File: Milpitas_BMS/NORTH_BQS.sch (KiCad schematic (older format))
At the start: 91 parts, among them U300 BQ79606

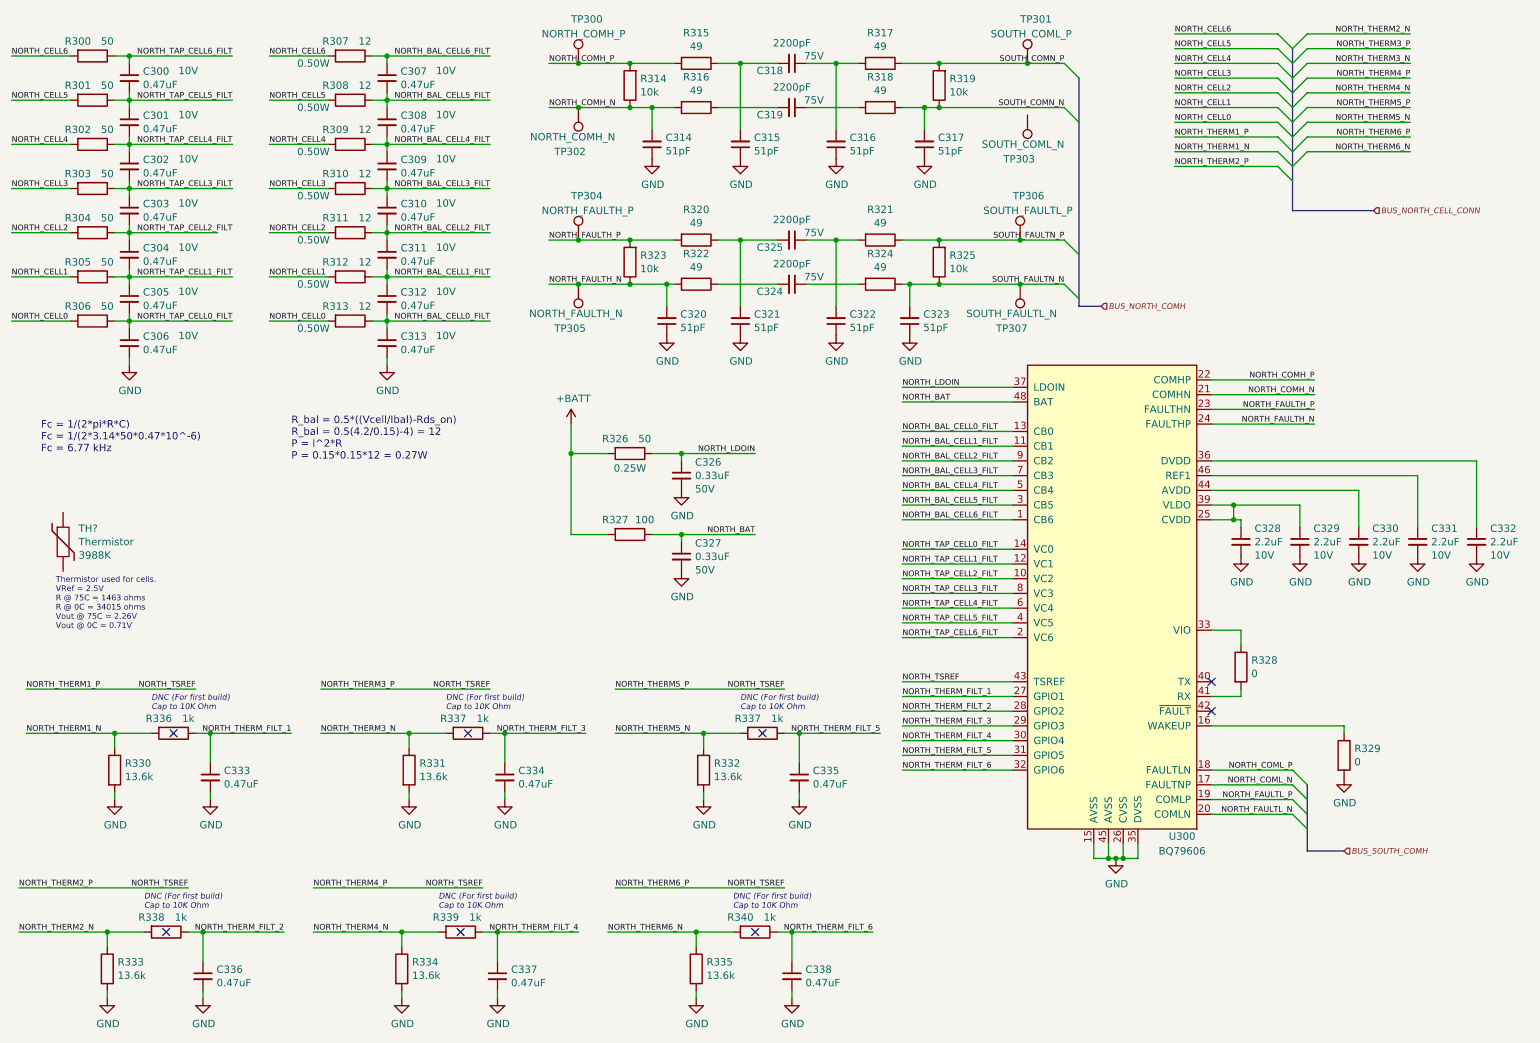
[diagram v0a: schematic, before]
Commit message: updated some parts to inclued footprints + digikey P/N
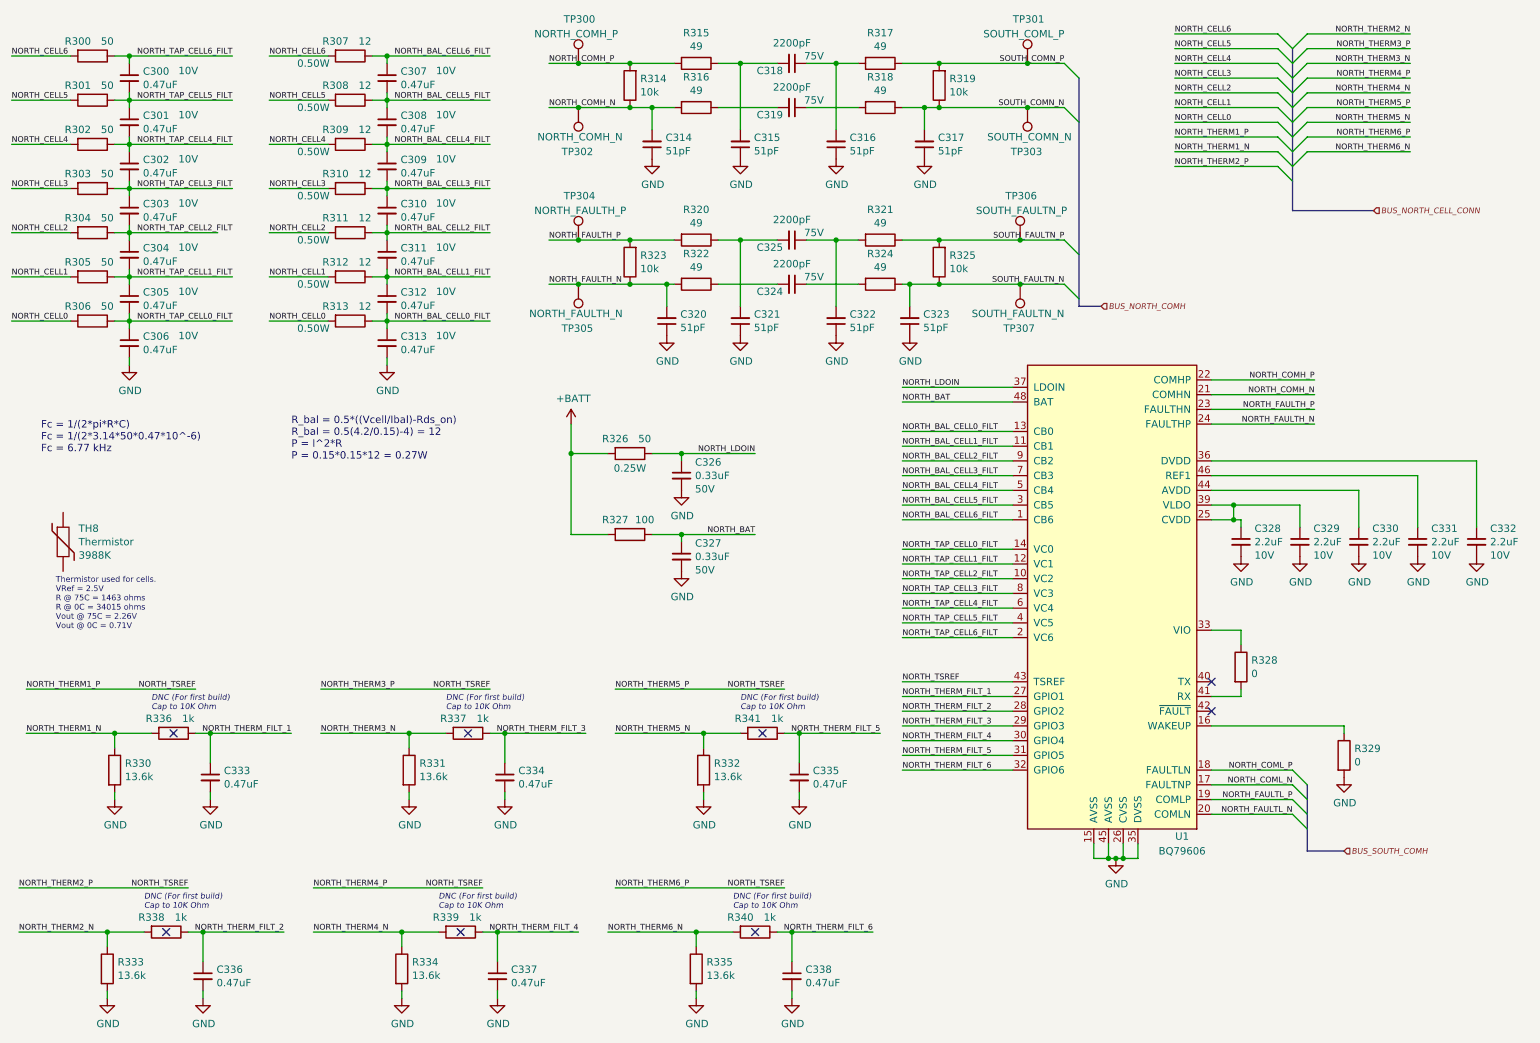
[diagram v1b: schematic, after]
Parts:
- removed U300: BQ79606, symbol Milipitas:BQ79606
- added U1: BQ79606, Package_QFP:LQFP-48-1EP_7x7mm_P0.5mm_EP3.6x3.6mm_ThermalVias, symbol Milipitas:BQ79606
- C300, C301, C302, C303, C304, C305, C306, C307, C308, C309, C310, C311, C312, C313, C314, C315, C316, C317, C318, C319, C320, C321, C322, C323, C324, C325, C326, C327, C328, C329, C330, C331, C332, C333, C334, C335, C336, C337, C338: footprint (none) -> Capacitor_SMD:C_0603_1608Metric
- R307, R308, R309, R310, R311, R312, R313, R314, R315, R316, R317, R318, R319, R320, R321, R322, R323, R324, R325, R326, R327, R328, R329, R336, R337, R338, R339, R340: footprint (none) -> Resistor_SMD:R_0603_1608Metric
- R341: renamed from R337; footprint (none) -> Resistor_SMD:R_0603_1608Metric
- TP300, TP301, TP302, TP304, TP305: footprint (none) -> TestPoint:TestPoint_Bridge_Pitch2.54mm_Drill1.0mm; Digikey (none) -> 36-5003-ND
- TP303: value SOUTH_COML_N -> SOUTH_COMN_N; footprint (none) -> TestPoint:TestPoint_Bridge_Pitch2.54mm_Drill1.0mm; Digikey (none) -> 36-5003-ND
- TP306: value SOUTH_FAULTL_P -> SOUTH_FAULTN_P; footprint (none) -> TestPoint:TestPoint_Bridge_Pitch2.54mm_Drill1.0mm; Digikey (none) -> 36-5003-ND
- TP307: value SOUTH_FAULTL_N -> SOUTH_FAULTN_N; footprint (none) -> TestPoint:TestPoint_Bridge_Pitch2.54mm_Drill1.0mm; Digikey (none) -> 36-5003-ND
- gave numbers to parts that had none: 1
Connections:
- net GND: now also U1.15 (AVSS), U1.26 (CVSS), U1.35 (DVSS), U1.45 (AVSS)
- net NORTH_BAL_CELL0_FILT: now also U1.13 (CB0)
- net NORTH_BAL_CELL1_FILT: now also U1.11 (CB1)
- net NORTH_BAL_CELL2_FILT: now also U1.9 (CB2)
- net NORTH_BAL_CELL3_FILT: now also U1.7 (CB3)
- net NORTH_BAL_CELL4_FILT: now also U1.5 (CB4)
- net NORTH_BAL_CELL5_FILT: now also U1.3 (CB5)
- net NORTH_BAL_CELL6_FILT: now also U1.1 (CB6)
- net NORTH_BAT: now also U1.48 (BAT)
- net NORTH_COMH_N: now also U1.21 (COMHN)
- net NORTH_COMH_P: now also U1.22 (COMHP)
- net NORTH_COML_N: now also U1.17 (FAULTNP)
- net NORTH_COML_P: now also U1.18 (FAULTLN)
- net NORTH_FAULTH_N: now also U1.24 (FAULTHP)
- net NORTH_FAULTH_P: now also U1.23 (FAULTHN)
- net NORTH_FAULTL_N: now also U1.20 (COMLN)
- net NORTH_FAULTL_P: now also U1.19 (COMLP)
- net NORTH_LDOIN: now also U1.37 (LDOIN)
- net NORTH_TAP_CELL0_FILT: now also U1.14 (VC0)
- net NORTH_TAP_CELL1_FILT: now also U1.12 (VC1)
- net NORTH_TAP_CELL2_FILT: now also U1.10 (VC2)
- net NORTH_TAP_CELL3_FILT: now also U1.8 (VC3)
- net NORTH_TAP_CELL4_FILT: now also U1.6 (VC4)
- net NORTH_TAP_CELL5_FILT: now also U1.4 (VC5)
- net NORTH_TAP_CELL6_FILT: now also U1.2 (VC6)
- net NORTH_THERM1_P: now also U1.43 (TSREF)
- net NORTH_THERM_FILT_1: now also U1.27 (GPIO1)
- net NORTH_THERM_FILT_2: now also U1.28 (GPIO2)
- net NORTH_THERM_FILT_3: now also U1.29 (GPIO3)
- net NORTH_THERM_FILT_4: now also U1.30 (GPIO4)
- net NORTH_THERM_FILT_5: now also U1.31 (GPIO5)
- net NORTH_THERM_FILT_6: now also U1.32 (GPIO6)
- net SOUTH_COMN_N: now also TP303.1
- net at C328.1, C329.1: now also U1.25 (CVDD), U1.39 (VLDO)
- net at C330.1: now also U1.44 (AVDD)
- net at C332.1: now also U1.36 (DVDD)
- net at C331.1: now also U1.46 (REF1)
- net at R329.1: now also U1.16 (WAKEUP)
- net at R328.1: now also U1.33 (VIO)
- net at R328.2: now also U1.41 (RX)

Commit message: lots of little fixes
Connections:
- net NORTH_CELL5 is gone; now on net NORTH_CELL_5: R301.2, R308.2
- net GND: no longer C306.2, C313.2, C314.1, C315.1, C320.1, C321.1, C326.2, C327.2, C328.2, C329.2, C330.2, C331.2, C332.2, C333.2, C334.2, C335.2, C336.2, C337.2, C338.2, R329.2, R330.2, R331.2, R332.2, R333.2, R334.2, R335.2, U1.15 (AVSS), U1.26 (CVSS), U1.35 (DVSS), U1.45 (AVSS)
- net NORTH_CELL0 renamed NORTH_CELL_0
- net NORTH_CELL1 renamed SOUTH_CELL_1
- net NORTH_CELL2 renamed NORTH_CELL_2
- net NORTH_CELL3 renamed NORTH_CELL_3
- net NORTH_CELL4 renamed NORTH_CELL_5
- net NORTH_CELL6 renamed NORTH_CELL_6
- new net GNDS: C306.2, C313.2, C314.1, C315.1, C320.1, C321.1, C326.2, C327.2, C328.2, C329.2, C330.2, C331.2, C332.2, C333.2, C334.2, C335.2, C336.2, C337.2, C338.2, R329.2, R330.2, R331.2, R332.2, R333.2, R334.2, R335.2, U1.15 (AVSS), U1.26 (CVSS), U1.35 (DVSS), U1.45 (AVSS)

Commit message: For review call
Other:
- moved on the sheet: R329
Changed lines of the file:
@@
 $Comp
 L Device:C_Small C?
-U 1 1 614FF6D3
-P 3500 2200
-AR Path="/614FF6D3" Ref="C?"  Part="1"
-AR Path="/5FBE719C/614FF6D3" Ref="C?"  Part="1"
-AR Path="/5FCA7CA4/614FF6D3" Ref="C?"  Part="1"
-AR Path="/614D0E92/614FF6D3" Ref="C311"  Part="1"
-F 0 "C311" H 3592 2246 50  0000 L CNN
-F 1 "0.47uF" H 3592 2155 50  0000 L CNN
-F 2 "Capacitor_SMD:C_0603_1608Metric" H 3500 2200 50  0001 C CNN
-F 3 "~" H 3500 2200 50  0001 C CNN
-F 4 "10V" H 3900 2250 50  0000 C CNN "Voltage"
-	1    3500 2200
-	1    0    0    -1
-$EndComp
-$Comp
-L Device:C_Small C?
 U 1 1 614FF6DA
 P 3500 2500
@@
 Wire Wire Line
 	6550 2100 6700 2100
-Entry Wire Line
-	8100 900  8200 1000
-Entry Wire Line
-	8100 1200 8200 1300
-Entry Wire Line
-	8100 2100 8200 2200
-Entry Wire Line
-	8100 2400 8200 2500
-Wire Bus Line
-	8200 2550 8350 2550
-Text HLabel 8350 2550 2    39   Input Italic 0
-BUS_NORTH_COMH
 Text Label 4600 900  0    39   ~ 0
 NORTH_COMH_P
@@
 Wire Wire Line
 	8300 6200 8300 6300
-Text HLabel 10000 6250 2    39   Input Italic 0
-BUS_SOUTH_COMH
-Wire Wire Line
-	10000 5400 10000 5450
-Wire Wire Line
-	9100 5400 10000 5400
 $Comp
 L Device:R R?
 U 1 1 614FFB13
-P 10000 5600
+P 10700 5650
 AR Path="/5FCA7CA4/614FFB13" Ref="R?"  Part="1"
 AR Path="/614D0E92/614FFB13" Ref="R329"  Part="1"
-F 0 "R329" H 10070 5646 50  0000 L CNN
-F 1 "0" H 10070 5555 50  0000 L CNN
-F 2 "Resistor_SMD:R_0603_1608Metric" V 9930 5600 50  0001 C CNN
-F 3 "~" H 10000 5600 50  0001 C CNN
-	1    10000 5600
+F 0 "R329" H 10770 5696 50  0000 L CNN
+F 1 "0" H 10770 5605 50  0000 L CNN
+F 2 "Resistor_SMD:R_0603_1608Metric" V 10630 5650 50  0001 C CNN
+F 3 "~" H 10700 5650 50  0001 C CNN
+	1    10700 5650
 	1    0    0    -1
 $EndComp
@@
 Text Label 9650 5700 2    39   ~ 0
 NORTH_COML_P
-Text Label 9650 5800 2    39   ~ 0
-NORTH_COML_N
 Text Label 9650 5900 2    39   ~ 0
 NORTH_FAULTL_P
 Text Label 9650 6000 2    39   ~ 0
 NORTH_FAULTL_N
-Wire Bus Line
-	9750 6250 10000 6250
-Entry Wire Line
-	9650 6000 9750 6100
-Entry Wire Line
-	9650 5900 9750 6000
-Entry Wire Line
-	9650 5800 9750 5900
-Entry Wire Line
-	9650 5700 9750 5800
 Wire Wire Line
 	9100 6000 9650 6000
@@
 L power:GNDS #PWR0233
 U 1 1 5E8477D6
-P 10000 5750
-F 0 "#PWR0233" H 10000 5500 50  0001 C CNN
-F 1 "GNDS" H 10005 5577 50  0000 C CNN
-F 2 "" H 10000 5750 50  0001 C CNN
-F 3 "" H 10000 5750 50  0001 C CNN
-	1    10000 5750
+P 10700 5800
+F 0 "#PWR0233" H 10700 5550 50  0001 C CNN
+F 1 "GNDS" H 10705 5627 50  0000 C CNN
+F 2 "" H 10700 5800 50  0001 C CNN
+F 3 "" H 10700 5800 50  0001 C CNN
+	1    10700 5800
 	1    0    0    -1
 $EndComp
@@
 Text GLabel 9800 1750 2    39   Input ~ 0
 NORTH_THERM2_N
-Wire Bus Line
-	8200 1000 8200 2550
-Wire Bus Line
-	9750 5800 9750 6250
+$Comp
+L Device:C_Small C?
+U 1 1 614FF6D3
+P 3500 2200
+AR Path="/614FF6D3" Ref="C?"  Part="1"
+AR Path="/5FBE719C/614FF6D3" Ref="C?"  Part="1"
+AR Path="/5FCA7CA4/614FF6D3" Ref="C?"  Part="1"
+AR Path="/614D0E92/614FF6D3" Ref="C311"  Part="1"
+F 0 "C311" H 3592 2246 50  0000 L CNN
+F 1 "0.47uF" H 3592 2155 50  0000 L CNN
+F 2 "Capacitor_SMD:C_0603_1608Metric" H 3500 2200 50  0001 C CNN
+F 3 "~" H 3500 2200 50  0001 C CNN
+F 4 "10V" H 3900 2250 50  0000 C CNN "Voltage"
+	1    3500 2200
+	1    0    0    -1
+$EndComp
+Wire Wire Line
+	10700 5400 10700 5500
+Wire Wire Line
+	9100 5400 10700 5400
+Text GLabel 9650 5700 2    39   Input ~ 0
+NORTH_COML_P
+Text GLabel 9650 5800 2    39   Input ~ 0
+NORTH_COML_N
+Text GLabel 9650 5900 2    39   Input ~ 0
+NORTH_FAULTL_P
+Text GLabel 9650 6000 2    39   Input ~ 0
+NORTH_FAULTL_N
+Text Label 9650 5800 2    39   ~ 0
+NORTH_COML_N
+Text GLabel 8100 900  2    39   Input ~ 0
+SOUTH_COMN_P
+Text GLabel 8100 1200 2    39   Input ~ 0
+SOUTH_COMN_N
+Text GLabel 8100 2100 2    39   Input ~ 0
+SOUTH_FAULTN_P
+Text GLabel 8100 2400 2    39   Input ~ 0
+SOUTH_FAULTN_N
 $EndSCHEMATC

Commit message: prelim layout ???
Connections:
- net NORTH_TAP_CELL2_FILT: now also C303.2, C304.1, R304.1
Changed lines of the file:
@@
 	1750 1750 2450 1750
 Wire Wire Line
-	1750 2050 2350 2050
+	1750 2050 2450 2050
 Wire Wire Line
 	1750 2350 2450 2350

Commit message: (maybe) final placement V1,0
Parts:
- removed TP300: NORTH_COMH_P, TestPoint:TestPoint_Bridge_Pitch2.54mm_Drill1.0mm, symbol Connector:TestPoint
- removed TP301: SOUTH_COML_P, TestPoint:TestPoint_Bridge_Pitch2.54mm_Drill1.0mm, symbol Connector:TestPoint
- removed TP302: NORTH_COMH_N, TestPoint:TestPoint_Bridge_Pitch2.54mm_Drill1.0mm, symbol Connector:TestPoint
- removed TP303: SOUTH_COMN_N, TestPoint:TestPoint_Bridge_Pitch2.54mm_Drill1.0mm, symbol Connector:TestPoint
- removed TP304: NORTH_FAULTH_P, TestPoint:TestPoint_Bridge_Pitch2.54mm_Drill1.0mm, symbol Connector:TestPoint
- removed TP305: NORTH_FAULTH_N, TestPoint:TestPoint_Bridge_Pitch2.54mm_Drill1.0mm, symbol Connector:TestPoint
- removed TP306: SOUTH_FAULTN_P, TestPoint:TestPoint_Bridge_Pitch2.54mm_Drill1.0mm, symbol Connector:TestPoint
- removed TP307: SOUTH_FAULTN_N, TestPoint:TestPoint_Bridge_Pitch2.54mm_Drill1.0mm, symbol Connector:TestPoint
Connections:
- net N_COMH_LS_P: now reaches C315.2, C318.2, R315.1
- net N_COMH_LS_N: now reaches C319.2, R316.1
- net N_FAULTH_LS_P: now reaches C321.2, C325.2, R320.1
- net N_FAULTH_LS_N: now reaches C324.2, R322.1
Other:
- moved on the sheet: R317, R318, R321, R324

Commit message: First pass routing
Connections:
- net +BATT is gone; now on net NORTH_CELL_6: R326.2, R327.2
- net NORTH_CELL_5: no longer R302.2, R309.2
- net SOUTH_CELL_1 renamed NORTH_CELL_1
- new net NORTH_CELL_4: R302.2, R309.2
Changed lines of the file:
@@
 Fc = 1/(2*pi*R*C)\nFc = 1/(2*3.14*50*0.47*10^-6)\nFc = 6.77 kHz\n
 $Comp
-L power:+BATT #PWR?
-U 1 1 614FF868
-P 4750 3350
-AR Path="/614FF868" Ref="#PWR?"  Part="1"
-AR Path="/5FBE719C/614FF868" Ref="#PWR?"  Part="1"
-AR Path="/5FCA7CA4/614FF868" Ref="#PWR?"  Part="1"
-AR Path="/614D0E92/614FF868" Ref="#PWR0204"  Part="1"
-F 0 "#PWR0204" H 4750 3200 50  0001 C CNN
-F 1 "+BATT" H 4765 3523 50  0000 C CNN
-F 2 "" H 4750 3350 50  0001 C CNN
-F 3 "" H 4750 3350 50  0001 C CNN
-	1    4750 3350
-	1    0    0    -1
-$EndComp
-$Comp
 L Device:R R?
 U 1 1 614FF86F
@@
 	10900 3600 10900 4050
 $Bitmap
-Pos 9400 6850
+Pos 9300 6850
 Scale 1.000000
 Data
@@
 NORTH_CELL_5
 Text GLabel 9800 950  2    39   Input ~ 0
-NORTH_CELL_5
+NORTH_CELL_4
 Text GLabel 9800 1050 2    39   Input ~ 0
 NORTH_CELL_3
@@
 NORTH_CELL_2
 Text GLabel 9800 1250 2    39   Input ~ 0
-SOUTH_CELL_1
+NORTH_CELL_1
 Text GLabel 9800 1350 2    39   Input ~ 0
 NORTH_CELL_0
@@
 Wire Wire Line
 	4600 2400 5150 2400
+Text Label 4400 3350 0    39   ~ 0
+NORTH_CELL6
+Wire Wire Line
+	4750 3350 4400 3350
 $EndSCHEMATC
